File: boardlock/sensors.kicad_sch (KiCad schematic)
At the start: 16 parts, among them Q2 Q_NPN_BCE, Q3 Q_NPN_BCE, Q4 BSS84PWH6327XTSA1, U1 LSM6DSO32, U3 SAM-M8Q

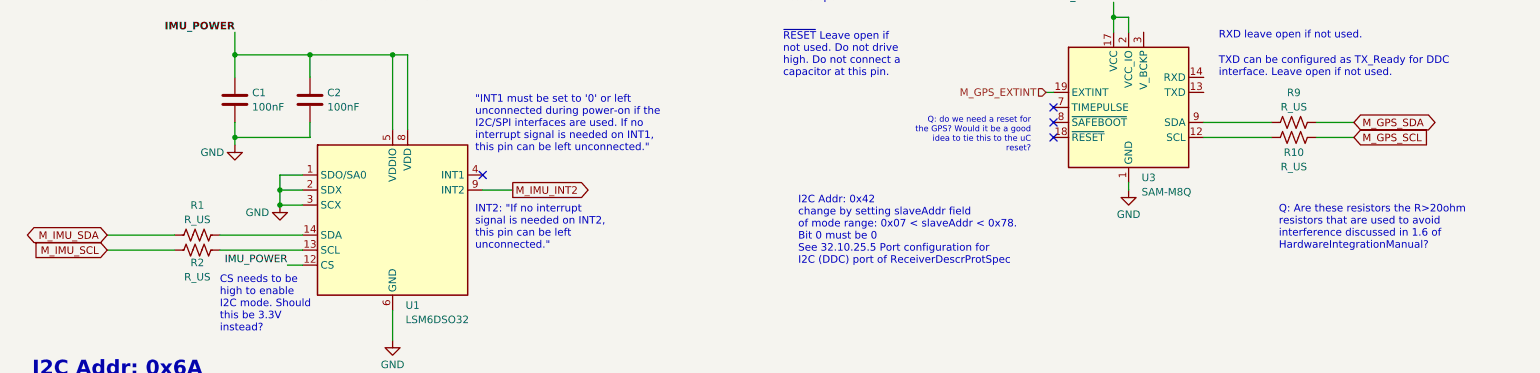
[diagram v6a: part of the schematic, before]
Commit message: added SPI and SD connections
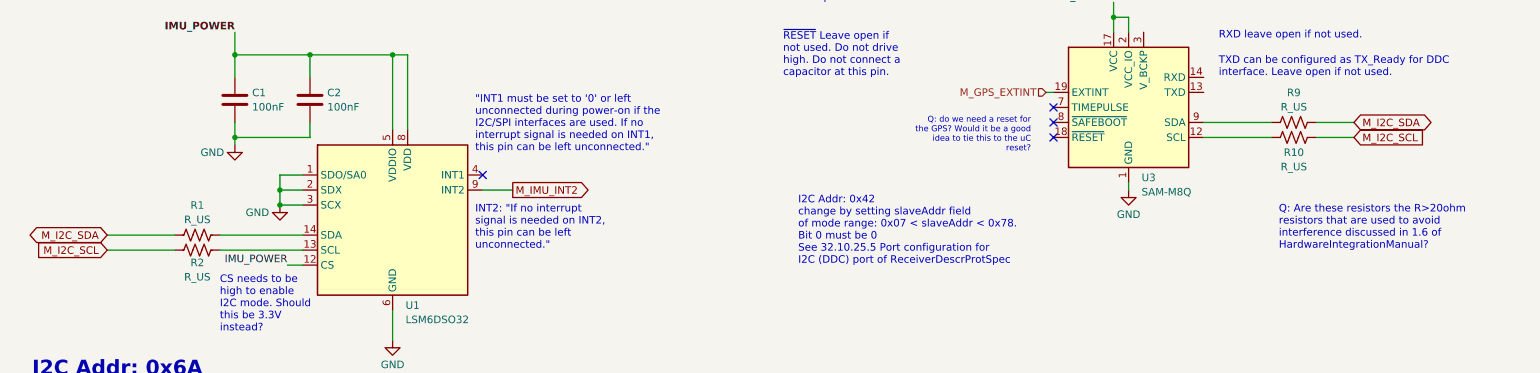
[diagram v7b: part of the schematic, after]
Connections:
- net M_IMU_SCL is gone; now on net M_I2C_SCL: R2.1
- net M_IMU_SDA is gone; now on net M_I2C_SDA: R1.1
- net M_GPS_SCL renamed M_I2C_SCL
- net M_GPS_SDA renamed M_I2C_SDA
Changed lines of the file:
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@@
     )
   )
-  (global_label "M_IMU_SCL" (shape input) (at 40.64 143.51 180) (fields_autoplaced)
+  (global_label "M_I2C_SCL" (shape input) (at 40.64 143.51 180) (fields_autoplaced)
     (effects (font (size 1.27 1.27)) (justify right))
-    (property "Intersheetrefs" "${INTERSHEET_REFS}" (at 27.3739 143.51 0)
+    (property "Intersheetrefs" "${INTERSHEET_REFS}" (at 27.7557 143.51 0)
       (effects (font (size 1.27 1.27)) (justify right) hide)
     )
   )
-  (global_label "M_GPS_SDA" (shape bidirectional) (at 251.46 121.92 0) (fields_autoplaced)
+  (global_label "M_I2C_SDA" (shape bidirectional) (at 251.46 121.92 0) (fields_autoplaced)
     (effects (font (size 1.27 1.27)) (justify left))
-    (property "Intersheetrefs" "${INTERSHEET_REFS}" (at 266.2607 121.92 0)
+    (property "Intersheetrefs" "${INTERSHEET_REFS}" (at 265.5161 121.92 0)
       (effects (font (size 1.27 1.27)) (justify left) hide)
     )
   )
-  (global_label "M_IMU_SDA" (shape bidirectional) (at 40.64 140.97 180) (fields_autoplaced)
+  (global_label "M_I2C_SDA" (shape bidirectional) (at 40.64 140.97 180) (fields_autoplaced)
     (effects (font (size 1.27 1.27)) (justify right))
-    (property "Intersheetrefs" "${INTERSHEET_REFS}" (at 26.2021 140.97 0)
+    (property "Intersheetrefs" "${INTERSHEET_REFS}" (at 26.5839 140.97 0)
       (effects (font (size 1.27 1.27)) (justify right) hide)
     )
   )
-  (global_label "M_GPS_SCL" (shape input) (at 251.46 124.46 0) (fields_autoplaced)
+  (global_label "M_I2C_SCL" (shape input) (at 251.46 124.46 0) (fields_autoplaced)
     (effects (font (size 1.27 1.27)) (justify left))
-    (property "Intersheetrefs" "${INTERSHEET_REFS}" (at 237.8311 124.46 0)
-      (effects (font (size 1.27 1.27)) (justify right) hide)
+    (property "Intersheetrefs" "${INTERSHEET_REFS}" (at 264.3443 124.46 0)
+      (effects (font (size 1.27 1.27)) (justify left) hide)
     )
   )

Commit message: modifications?
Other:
- note added: "CS needs to be high to enable I2C mode"
- note removed: "CS needs to be high to enable I2C mode. Should this be 3.3V instead?"
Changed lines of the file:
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@@
     (effects (font (size 1.27 1.27)) (justify left bottom))
   )
-  (text "CS needs to be \nhigh to enable \nI2C mode. Should \nthis be 3.3V \ninstead?"
-    (at 59.69 157.48 0)
+  (text "CS needs to be \nhigh to enable \nI2C mode" (at 59.69 152.4 0)
     (effects (font (size 1.27 1.27)) (justify left bottom))
   )
